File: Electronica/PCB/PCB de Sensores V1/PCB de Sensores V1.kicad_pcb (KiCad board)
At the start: 2 copper layers, 66.9 x 42.5 mm, 11 parts, among them J1 Conn_02x08_Odd_Even, U1 ULTRASONICO1, U2 ULTRASONICO2, U3 ULTRASONICO3, U4 ULTRASONICO4, U5 ULTRASONICO5

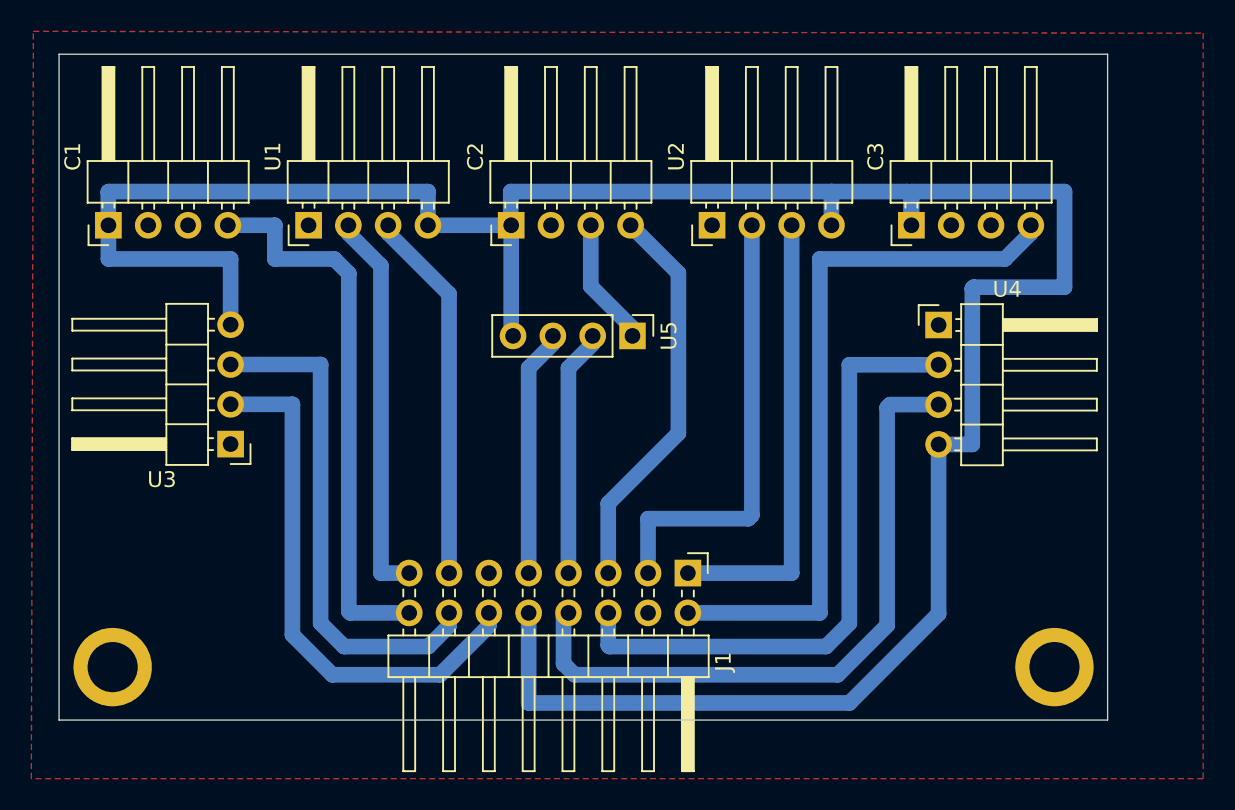
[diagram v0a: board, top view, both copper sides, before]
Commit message: PCB Sensores a modificar
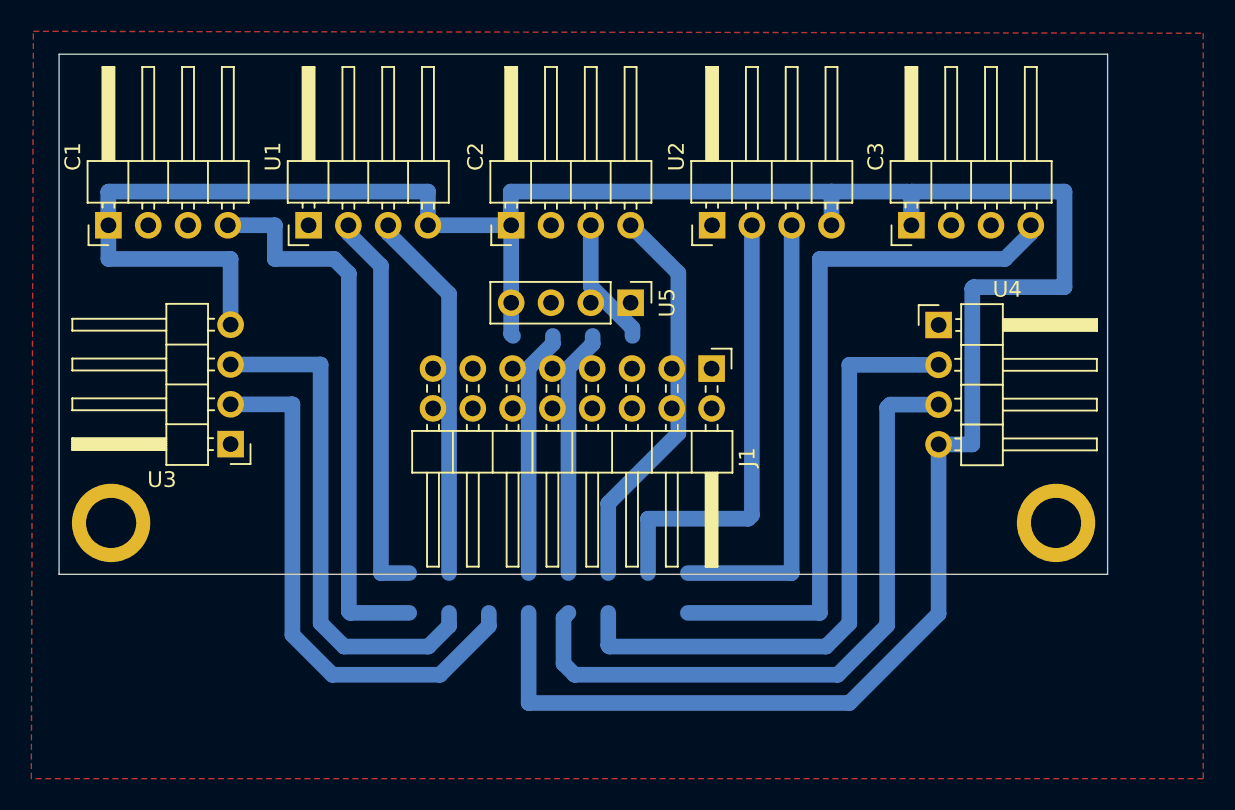
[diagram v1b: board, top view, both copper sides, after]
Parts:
- moved J1 13.1 mm to (214.4, 62.0)
- moved ? 9.20 mm to (176.1, 71.9)
- moved ? 9.20 mm to (236.4, 71.9)
- moved U5 2.12 mm to (209.2, 57.9)
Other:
- board size 66.9 x 42.5 mm -> 66.9 x 33.2 mm
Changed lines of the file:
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@@
 	(footprint "Connector_PinHeader_2.54mm:PinHeader_2x08_P2.54mm_Horizontal"
 		(layer "F.Cu")
-		(at 212.905 75.1 -90)
+		(at 214.42 62.05 -90)
 		(descr "Through hole angled pin header, 2x08, 2.54mm pitch, 6mm pin length, double rows")
 		(tags "Through hole angled pin header THT 2x08 2.54mm double row")
@@
 	(footprint ""
 		(layer "F.Cu")
-		(at 176.2 81.1)
+		(at 176.1 71.9)
 		(property "Reference" ""
 			(at 0 0 0)
@@
 	(footprint "Connector_PinHeader_2.54mm:PinHeader_1x04_P2.54mm_Vertical"
 		(layer "F.Cu")
-		(at 209.37 59.965 -90)
+		(at 209.25 57.85 -90)
 		(descr "Through hole straight pin header, 1x04, 2.54mm pitch, single row")
 		(tags "Through hole pin header THT 1x04 2.54mm single row")
@@
 	(footprint ""
 		(layer "F.Cu")
-		(at 236.3 81.1)
+		(at 236.4 71.9)
 		(property "Reference" ""
 			(at 0 0 0)
@@
 	(gr_rect
 		(start 172.78 41.99)
-		(end 239.69 84.48)
+		(end 239.69 75.18)
 		(stroke
 			(width 0.05)

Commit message: SELIGRAFIA
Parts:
- CNY 1: renamed from C1
- CNY 2: renamed from C2
- CNY 3: renamed from C3
- Conector 1: renamed from J1
- Ultrasonico 1: renamed from U1
- Ultrasonico 2: renamed from U2
- Ultrasonico 3: renamed from U3
- Ultrasonico 4: renamed from U4
- Ultrasonico 5: renamed from U5
- moved Conector 1 0.27 mm to (214.3, 61.8)
- moved Ultrasonico 5 0.23 mm to (209.2, 57.6)
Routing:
- net CNY3: track 45.7 -> 25.5 mm
- net +5V: track 164.2 -> 146.5 mm
- net TRIG2: track 28.8 -> 11.3 mm
- net ECHO2: track 28.7 -> 11.3 mm
- net ECHO4: track 40.3 -> 22.9 mm
- net TRIG4: track 42.9 -> 26.2 mm
- net CNY2: track 25.3 -> 9.88 mm
- net CNY1: track 35.7 -> 21.8 mm
- net TRIG3: track 32.4 -> 18.7 mm
- net ECHO1: track 24.9 -> 11.4 mm
- net ECHO3: track 34.4 -> 22.0 mm
- net TRIG1: track 23.8 -> 11.5 mm
- net TRIG5: track 15.8 -> 5.12 mm
- net ECHO5: track 15.8 -> 5.12 mm
- net GND: track 8.16 -> 0.00 mm

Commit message: Listo PCB Botones
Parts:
- moved Ultrasonico 4 2.86 mm to (226.1, 59.3)
- moved ? 2.81 mm to (233.6, 72.2)
- moved Ultrasonico 5 0.37 mm to (209.2, 57.2)
- moved ? 0.30 mm to (176.2, 72.2)
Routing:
- net +5V: track 146.5 -> 112.0 mm
- net ECHO3: track 22.0 -> 32.7 mm
- net TRIG3: track 18.7 -> 29.1 mm
- net CNY1: track 21.8 -> 32.1 mm
- net CNY3: track 25.5 -> 32.0 mm
- net TRIG2: track 11.3 -> 14.1 mm
- net ECHO2: track 11.3 -> 13.9 mm
- net TRIG1: track 11.5 -> 14.1 mm
- net ECHO1: track 11.4 -> 13.8 mm
- net CNY2: track 9.88 -> 12.0 mm
- net TRIG4: track 26.2 -> 27.7 mm
- net ECHO4: track 22.9 -> 24.1 mm
- added copper zone on B.Cu, net +5V
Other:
- board size 66.9 x 33.2 mm -> 63.5 x 32.9 mm
- board text added: "PCB Sensores V1"

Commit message: Codigo nuevo sin terminar
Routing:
- net GND: track 0.00 -> 184.3 mm, vias 0 -> 4
- net +5V: track 112.0 -> 191.5 mm, vias 0 -> 4
- net ECHO3: track 32.7 -> 28.0 mm
- net TRIG3: track 29.1 -> 24.9 mm
- net CNY1: track 32.1 -> 28.6 mm, vias 0 -> 2
- net CNY2: track 12.0 -> 12.7 mm
- removed copper zone on B.Cu, net +5V
- removed copper zone on F.Cu, net GND
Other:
- board size 63.5 x 32.9 mm -> 64.3 x 32.9 mm

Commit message: ?
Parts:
- removed CNY 1: CNY1, Connector_PinHeader_2.54mm:PinHeader_1x04_P2.54mm_Horizontal
- removed CNY 2: CNY2, Connector_PinHeader_2.54mm:PinHeader_1x04_P2.54mm_Horizontal
- removed CNY 3: CNY3, Connector_PinHeader_2.54mm:PinHeader_1x04_P2.54mm_Horizontal
- removed Conector 1: Conn_02x08_Odd_Even, Connector_PinHeader_2.54mm:PinHeader_2x08_P2.54mm_Horizontal
- removed Ultrasonico 1: ULTRASONICO1, Connector_PinHeader_2.54mm:PinHeader_1x04_P2.54mm_Horizontal
- removed Ultrasonico 2: ULTRASONICO2, Connector_PinHeader_2.54mm:PinHeader_1x04_P2.54mm_Horizontal
- removed Ultrasonico 3: ULTRASONICO3, Connector_PinHeader_2.54mm:PinHeader_1x04_P2.54mm_Horizontal
- removed Ultrasonico 4: ULTRASONICO4, Connector_PinHeader_2.54mm:PinHeader_1x04_P2.54mm_Horizontal
- removed Ultrasonico 5: ULTRASONICO5, Connector_PinHeader_2.54mm:PinHeader_1x04_P2.54mm_Vertical
- added C1: CNY1, Connector_PinHeader_2.54mm:PinHeader_1x04_P2.54mm_Horizontal, F.Cu at (200.6, 53.2)
- added C2: CNY2, Connector_PinHeader_2.54mm:PinHeader_1x04_P2.54mm_Horizontal, F.Cu at (227.4, 53.2)
- added C3: CNY3, Connector_PinHeader_2.54mm:PinHeader_1x04_P2.54mm_Horizontal, F.Cu at (175.8, 53.2)
- added J1: Conexion Sensores, Connector_PinHeader_2.54mm:PinHeader_2x08_P2.54mm_Horizontal, F.Cu at (213.2, 61.8)
- added U1: ULTRASONICO1, Connector_PinHeader_2.54mm:PinHeader_1x04_P2.54mm_Horizontal, F.Cu at (188.1, 53.3)
- added U2: ULTRASONICO2, Connector_PinHeader_2.54mm:PinHeader_1x04_P2.54mm_Horizontal, F.Cu at (213.0, 53.4)
- added U3: ULTRASONICO3, Connector_PinHeader_2.54mm:PinHeader_1x04_P2.54mm_Horizontal, F.Cu at (225.7, 58.9)
- added U4: ULTRASONICO4, Connector_PinHeader_2.54mm:PinHeader_1x04_P2.54mm_Horizontal, F.Cu at (184.2, 67.3)
- added U5: ULTRASONICO5, Connector_PinHeader_2.54mm:PinHeader_1x04_P2.54mm_Vertical, F.Cu at (208.2, 57.2)
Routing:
- net +5V: track 191.5 -> 43.0 mm, vias 4 -> 0
- net GND: track 184.3 -> 92.1 mm, vias 4 -> 0
- net CNY3: track 31.8 -> 0.00 mm
- net CNY1: track 28.6 -> 0.00 mm, vias 2 -> 0
- net ECHO3: track 28.0 -> 0.00 mm
- net TRIG4: track 27.7 -> 0.00 mm
- net TRIG3: track 24.9 -> 0.00 mm
- net ECHO4: track 24.1 -> 0.00 mm
- net CNY 3: track 0.00 -> 20.8 mm
- net TRIG 3: track 0.00 -> 20.3 mm
- net ECHO 3: track 0.00 -> 18.2 mm
- net TRIG1: track 14.2 -> 0.00 mm
- net TRIG2: track 14.1 -> 0.00 mm
- net ECHO2: track 13.9 -> 0.00 mm
- net ECHO1: track 13.8 -> 0.00 mm
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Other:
- board text removed: "PCB Sensores V1"

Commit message: ?
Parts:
- moved U5 20.3 mm to (190.5, 67.2), turned to 180 degrees
- moved U1 14.3 mm to (202.4, 53.4)
- moved C1 11.9 mm to (188.6, 53.4)
- moved U2 2.64 mm to (215.6, 53.3)
- moved U4 1.20 mm to (183.0, 67.2)
- moved C2 0.39 mm to (227.8, 53.4)
- moved C3 0.13 mm to (175.8, 53.4)
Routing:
- net +5V: track 43.0 -> 155.5 mm, vias 0 -> 8
- net CNY 2: track 0.00 -> 50.9 mm, vias 0 -> 2
- net ECHO 4: track 0.00 -> 41.9 mm
- net TRIG 4: track 0.00 -> 37.8 mm
- net TRIG 5: track 0.00 -> 28.3 mm
- net GND: track 92.1 -> 119.4 mm, vias 0 -> 3
- net CNY 1: track 0.00 -> 15.2 mm
- net TRIG 1: track 0.00 -> 8.67 mm
- net ECHO 1: track 0.00 -> 8.67 mm
- net ECHO 3: track 18.2 -> 15.2 mm
- net TRIG 3: track 20.3 -> 17.7 mm
- net ECHO 2: track 10.4 -> 13.0 mm
- net TRIG 2: track 10.4 -> 12.6 mm
- net CNY 3: track 20.8 -> 22.9 mm
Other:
- board size 64.3 x 32.9 mm -> 65.2 x 34.4 mm

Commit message: pcb sensores corregida
Tonto el que lee
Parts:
- U4: footprint Connector_PinHeader_2.54mm:PinHeader_1x04_P2.54mm_Horizontal -> Connector_PinHeader_2.54mm:PinHeader_1x04_P2.54mm_Vertical
- U5: footprint Connector_PinHeader_2.54mm:PinHeader_1x04_P2.54mm_Vertical -> Connector_PinHeader_2.54mm:PinHeader_1x04_P2.54mm_Horizontal
- moved C2 39.1 mm to (188.7, 53.4)
- moved C1 39.1 mm to (227.7, 53.4)
- moved U4 37.4 mm to (220.2, 70.8), turned to 90 degrees
- moved U5 7.09 mm to (183.4, 67.3)
- moved CONECTOR 1.52 mm to (214.6, 61.0)
- moved U1 0.70 mm to (201.7, 53.4)
- moved U2 0.44 mm to (215.2, 53.4)
- renumbered J1 to CONECTOR
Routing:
- net GND: track 119.4 -> 211.1 mm, vias 3 -> 12
- net CNY 1: track 15.2 -> 57.9 mm
- net CNY 2: track 50.9 -> 10.0 mm, vias 2 -> 0
- net ECHO 5: track 0.00 -> 26.0 mm
- net ECHO 4: track 41.9 -> 23.0 mm
- net TRIG 5: track 28.3 -> 21.9 mm
- net TRIG 4: track 37.8 -> 31.8 mm
- net +5V: track 155.5 -> 149.9 mm, vias 8 -> 2
- net ECHO 3: track 15.2 -> 13.5 mm
- net TRIG 1: track 8.67 -> 10.2 mm
- net ECHO 1: track 8.67 -> 10.2 mm
- net CNY 3: track 22.9 -> 21.6 mm
- net TRIG 2: track 12.6 -> 13.3 mm
- net TRIG 3: track 17.7 -> 16.9 mm
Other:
- board size 65.2 x 34.4 mm -> 65.2 x 34.7 mm
- board text added: "+"
- board text added: "-"
